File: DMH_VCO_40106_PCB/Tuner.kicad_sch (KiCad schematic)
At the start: 32 parts, among them J300 AVR-ISP-6, SW3 SW_SPDT_321_OnOff, U5 ATtiny4313-P, U6 SM420561N

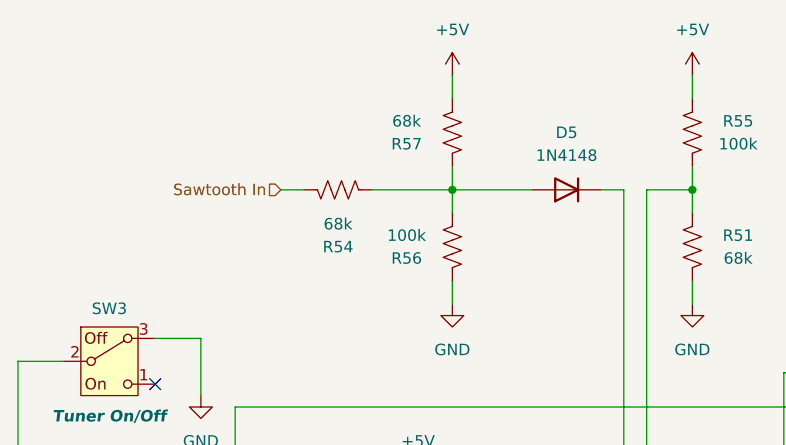
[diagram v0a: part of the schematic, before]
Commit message: FW work in progress
Code left in state where fixed frequency point (e.g. 300Hz) is recognized, and the tuner swings from TOO LOW to TOO HIGH depending if below or above this frequency. I see a ~+10Hz offset though if checking the frequency in ableton. Also had to connect uc to square wave. Saw wave is too unstable without hysteresis.
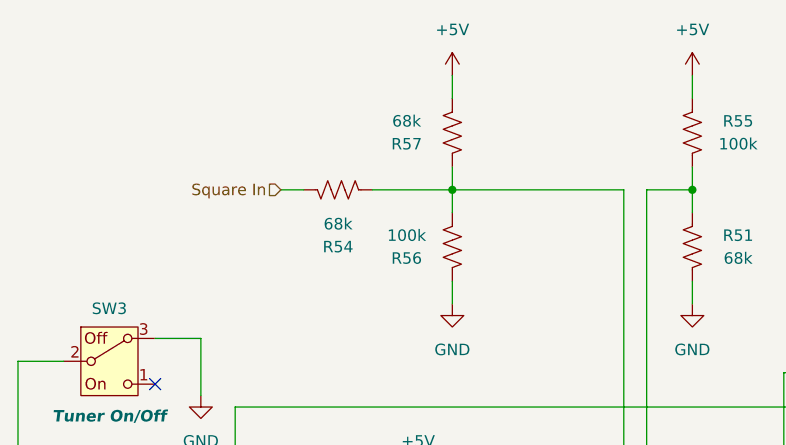
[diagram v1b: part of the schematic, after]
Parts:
- removed D5: 1N4148, Diode_THT:D_DO-35_SOD27_P7.62mm_Horizontal, symbol Diode:1N4148
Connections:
- net at U5.12 (PB0): now also R54.2, R56.1, R57.2
- net Sawtooth In renamed Square In
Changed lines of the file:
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@@
 	(wire
 		(pts
-			(xy 76.2 31.75) (xy 67.31 31.75)
+			(xy 67.31 31.75) (xy 86.36 31.75)
 		)
 		(stroke
@@
 	(wire
 		(pts
-			(xy 86.36 31.75) (xy 83.82 31.75)
-		)
-		(stroke
-			(width 0)
-			(type default)
-		)
-	)
-	(wire
-		(pts
 			(xy 25.4 67.31) (xy 25.4 93.98)
 		)
@@
 		)
 	)
-	(hierarchical_label "Sawtooth In"
+	(hierarchical_label "Square In"
 		(shape input)
 		(at 48.26 31.75 180)
@@
 					(unit 1)
 				)
-			)
-		)
-	)
-	(symbol
-		(lib_id "Diode:1N4148")
-		(at 80.01 31.75 180)
-		(unit 1)
-		(exclude_from_sim no)
-		(in_bom yes)
-		(on_board yes)
-		(dnp no)
-		(fields_autoplaced yes)
-		(property "Reference" "D5"
-			(at 80.01 25.4 0)
-			(effects
-				(font
-					(size 1.27 1.27)
-				)
-			)
-		)
-		(property "Value" "1N4148"
-			(at 80.01 27.94 0)
-			(effects
-				(font
-					(size 1.27 1.27)
-				)
-			)
-		)
-		(property "Footprint" "Diode_THT:D_DO-35_SOD27_P7.62mm_Horizontal"
-			(at 80.01 31.75 0)
-			(effects
-				(font
-					(size 1.27 1.27)
-				)
-				(hide yes)
-			)
-		)
-		(property "Datasheet" "https://assets.nexperia.com/documents/data-sheet/1N4148_1N4448.pdf"
-			(at 80.01 31.75 0)
-			(effects
-				(font
-					(size 1.27 1.27)
-				)
-				(hide yes)
-			)
-		)
-		(property "Description" "100V 0.15A standard switching diode, DO-35"
-			(at 80.01 31.75 0)
-			(effects
-				(font
-					(size 1.27 1.27)
-				)
-				(hide yes)
-			)
-		)
-		(property "Sim.Device" "D"
-			(at 80.01 31.75 0)
-			(effects
-				(font
-					(size 1.27 1.27)
-				)
-				(hide yes)
-			)
-		)
-		(property "Sim.Pins" "1=K 2=A"
-			(at 80.01 31.75 0)
-			(effects
-				(font
-					(size 1.27 1.27)
-				)
-				(hide yes)
-			)
-		)
-		(pin "1"
-		)
-		(pin "2"
-		)
-		(instances
-			(project "DMH_VCO_40106_PCB"
-				(path "/fefed352-c100-4617-bbfb-c55e7427b122/ec8b77a2-f589-4806-8224-6b0ccc79bab4"
-					(reference "D5")
-					(unit 1)
-				)

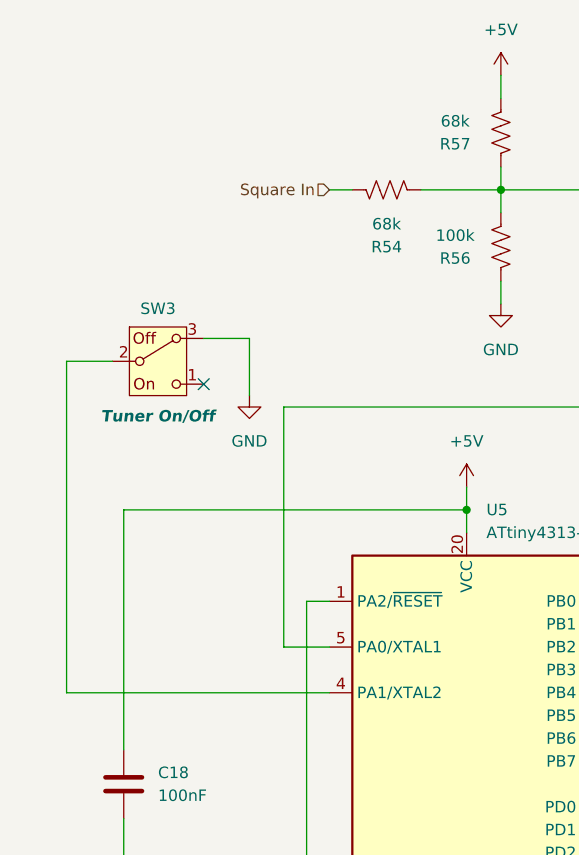
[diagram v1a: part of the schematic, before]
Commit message: Added pull up resistor to tuner switch
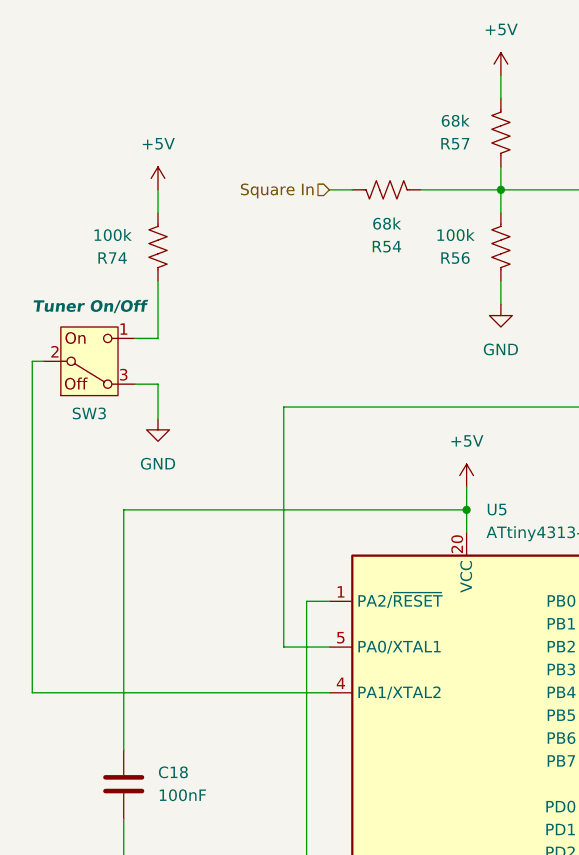
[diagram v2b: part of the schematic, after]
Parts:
- added R74: 100k, Resistor_THT:R_Axial_DIN0207_L6.3mm_D2.5mm_P7.62mm_Horizontal, symbol Device:R_US
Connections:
- net +5V: now also R74.1
- net at SW3.1 (C): now also R74.2
- no-connect marks 1 -> 0
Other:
- moved on the sheet: SW3
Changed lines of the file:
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@@
 		(color 0 0 0 0)
 	)
-	(no_connect
-		(at 34.29 53.34)
-	)
 	(wire
 		(pts
@@
 	(wire
 		(pts
-			(xy 39.37 48.26) (xy 34.29 48.26)
-		)
-		(stroke
-			(width 0)
-			(type default)
-		)
-	)
-	(wire
-		(pts
 			(xy 170.18 62.23) (xy 170.18 69.85)
 		)
@@
 	(wire
 		(pts
-			(xy 39.37 54.61) (xy 39.37 48.26)
+			(xy 29.21 57.15) (xy 29.21 53.34)
 		)
 		(stroke
@@
 	(wire
 		(pts
-			(xy 19.05 87.63) (xy 48.26 87.63)
+			(xy 15.24 87.63) (xy 48.26 87.63)
 		)
 		(stroke
@@
 	(wire
 		(pts
+			(xy 29.21 48.26) (xy 29.21 41.91)
+		)
+		(stroke
+			(width 0)
+			(type default)
+		)
+	)
+	(wire
+		(pts
 			(xy 35.56 163.83) (xy 66.04 163.83)
 		)
@@
 	(wire
 		(pts
-			(xy 24.13 50.8) (xy 19.05 50.8)
+			(xy 16.51 50.8) (xy 15.24 50.8)
 		)
 		(stroke
@@
 	(wire
 		(pts
-			(xy 19.05 50.8) (xy 19.05 87.63)
+			(xy 15.24 50.8) (xy 15.24 87.63)
 		)
 		(stroke
@@
 	(wire
 		(pts
+			(xy 29.21 31.75) (xy 29.21 34.29)
+		)
+		(stroke
+			(width 0)
+			(type default)
+		)
+	)
+	(wire
+		(pts
 			(xy 162.56 146.05) (xy 162.56 158.75)
 		)
@@
 	(wire
 		(pts
+			(xy 29.21 53.34) (xy 26.67 53.34)
+		)
+		(stroke
+			(width 0)
+			(type default)
+		)
+	)
+	(wire
+		(pts
 			(xy 127 175.26) (xy 127 177.8)
 		)
@@
 		)
 	)
+	(wire
+		(pts
+			(xy 26.67 48.26) (xy 29.21 48.26)
+		)
+		(stroke
+			(width 0)
+			(type default)
+		)
+	)
 	(hierarchical_label "Square In"
 		(shape input)
@@
 	(symbol
 		(lib_id "SynthStuff:SW_SPDT_321_OnOff")
-		(at 29.21 50.8 0)
+		(at 21.59 50.8 0)
+		(mirror x)
 		(unit 1)
 		(exclude_from_sim no)
@@
 		(dnp no)
 		(property "Reference" "SW3"
-			(at 29.21 44.958 0)
+			(at 21.59 56.642 0)
 			(effects
 				(font
@@
 		)
 		(property "Value" "SW_SPDT_321_OnOff"
-			(at 29.21 55.88 0)
+			(at 21.59 45.72 0)
 			(effects
 				(font
@@
 		)
 		(property "Footprint" "SynthStuff:Toggle_Switch_THT"
-			(at 29.21 60.96 0)
+			(at 21.59 40.64 0)
 			(effects
 				(font
@@
 		)
 		(property "Datasheet" "~"
-			(at 29.21 58.42 0)
+			(at 21.59 43.18 0)
 			(effects
 				(font
@@
 		)
 		(property "Description" "Switch, single pole double throw"
-			(at 29.21 50.8 0)
+			(at 21.59 50.8 0)
 			(effects
 				(font
@@
 		)
 		(property "Function" "Tuner On/Off"
-			(at 29.21 56.896 0)
+			(at 21.59 44.704 0)
 			(effects
 				(font
@@
 	(symbol
 		(lib_id "power:GND")
-		(at 39.37 54.61 0)
+		(at 29.21 57.15 0)
 		(unit 1)
 		(exclude_from_sim no)
@@
 		(fields_autoplaced yes)
 		(property "Reference" "#PWR011"
-			(at 39.37 60.96 0)
+			(at 29.21 63.5 0)
 			(effects
 				(font
@@
 		)
 		(property "Value" "GND"
-			(at 39.37 59.69 0)
+			(at 29.21 62.23 0)
 			(effects
 				(font
@@
 		)
 		(property "Footprint" ""
-			(at 39.37 54.61 0)
+			(at 29.21 57.15 0)
 			(effects
 				(font
@@
 		)
 		(property "Datasheet" ""
-			(at 39.37 54.61 0)
+			(at 29.21 57.15 0)
 			(effects
 				(font
@@
 		)
 		(property "Description" "Power symbol creates a global label with name \"GND\" , ground"
-			(at 39.37 54.61 0)
+			(at 29.21 57.15 0)
 			(effects
 				(font
@@
 	)
 	(symbol
+		(lib_id "power:+5V")
+		(at 29.21 31.75 0)
+		(unit 1)
+		(exclude_from_sim no)
+		(in_bom yes)
+		(on_board yes)
+		(dnp no)
+		(fields_autoplaced yes)
+		(property "Reference" "#PWR013"
+			(at 29.21 35.56 0)
+			(effects
+				(font
+					(size 1.27 1.27)
+				)
+				(hide yes)
+			)
+		)
+		(property "Value" "+5V"
+			(at 29.21 26.67 0)
+			(effects
+				(font
+					(size 1.27 1.27)
+				)
+			)
+		)
+		(property "Footprint" ""
+			(at 29.21 31.75 0)
+			(effects
+				(font
+					(size 1.27 1.27)
+				)
+				(hide yes)
+			)
+		)
+		(property "Datasheet" ""
+			(at 29.21 31.75 0)
+			(effects
+				(font
+					(size 1.27 1.27)
+				)
+				(hide yes)
+			)
+		)
+		(property "Description" "Power symbol creates a global label with name \"+5V\""
+			(at 29.21 31.75 0)
+			(effects
+				(font
+					(size 1.27 1.27)
+				)
+				(hide yes)
+			)
+		)
+		(pin "1"
+		)
+		(instances
+			(project "DMH_VCO_40106_PCB"
+				(path "/fefed352-c100-4617-bbfb-c55e7427b122/ec8b77a2-f589-4806-8224-6b0ccc79bab4"
+					(reference "#PWR013")
+					(unit 1)
+				)
+			)
+		)
+	)
+	(symbol
 		(lib_id "Device:R_US")
 		(at 160.02 52.07 90)
@@
 					(unit 1)
 				)
+			)
+		)
+	)
+	(symbol
+		(lib_id "Device:R_US")
+		(at 29.21 38.1 0)
+		(mirror y)
+		(unit 1)
+		(exclude_from_sim no)
+		(in_bom yes)
+		(on_board yes)
+		(dnp no)
+		(property "Reference" "R74"
+			(at 24.13 39.37 0)
+			(effects
+				(font
+					(size 1.27 1.27)
+				)
+			)
+		)
+		(property "Value" "100k"
+			(at 24.13 36.83 0)
+			(effects
+				(font
+					(size 1.27 1.27)
+				)
+			)
+		)
+		(property "Footprint" "Resistor_THT:R_Axial_DIN0207_L6.3mm_D2.5mm_P7.62mm_Horizontal"
+			(at 28.194 38.354 90)
+			(effects
+				(font
+					(size 1.27 1.27)
+				)
+				(hide yes)
+			)
+		)
+		(property "Datasheet" "~"
+			(at 29.21 38.1 0)
+			(effects
+				(font
+					(size 1.27 1.27)
+				)
+				(hide yes)
+			)
+		)
+		(property "Description" "Resistor, US symbol"
+			(at 29.21 38.1 0)
+			(effects
+				(font
+					(size 1.27 1.27)
+				)
+				(hide yes)
+			)
+		)
+		(pin "2"
+		)
+		(pin "1"
+		)
+		(instances
+			(project "DMH_VCO_40106_PCB"
+				(path "/fefed352-c100-4617-bbfb-c55e7427b122/ec8b77a2-f589-4806-8224-6b0ccc79bab4"
+					(reference "R74")
+					(unit 1)
+				)
